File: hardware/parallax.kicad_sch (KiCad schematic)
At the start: 18 parts, among them U1 4052, U2 MCP6002-xMC

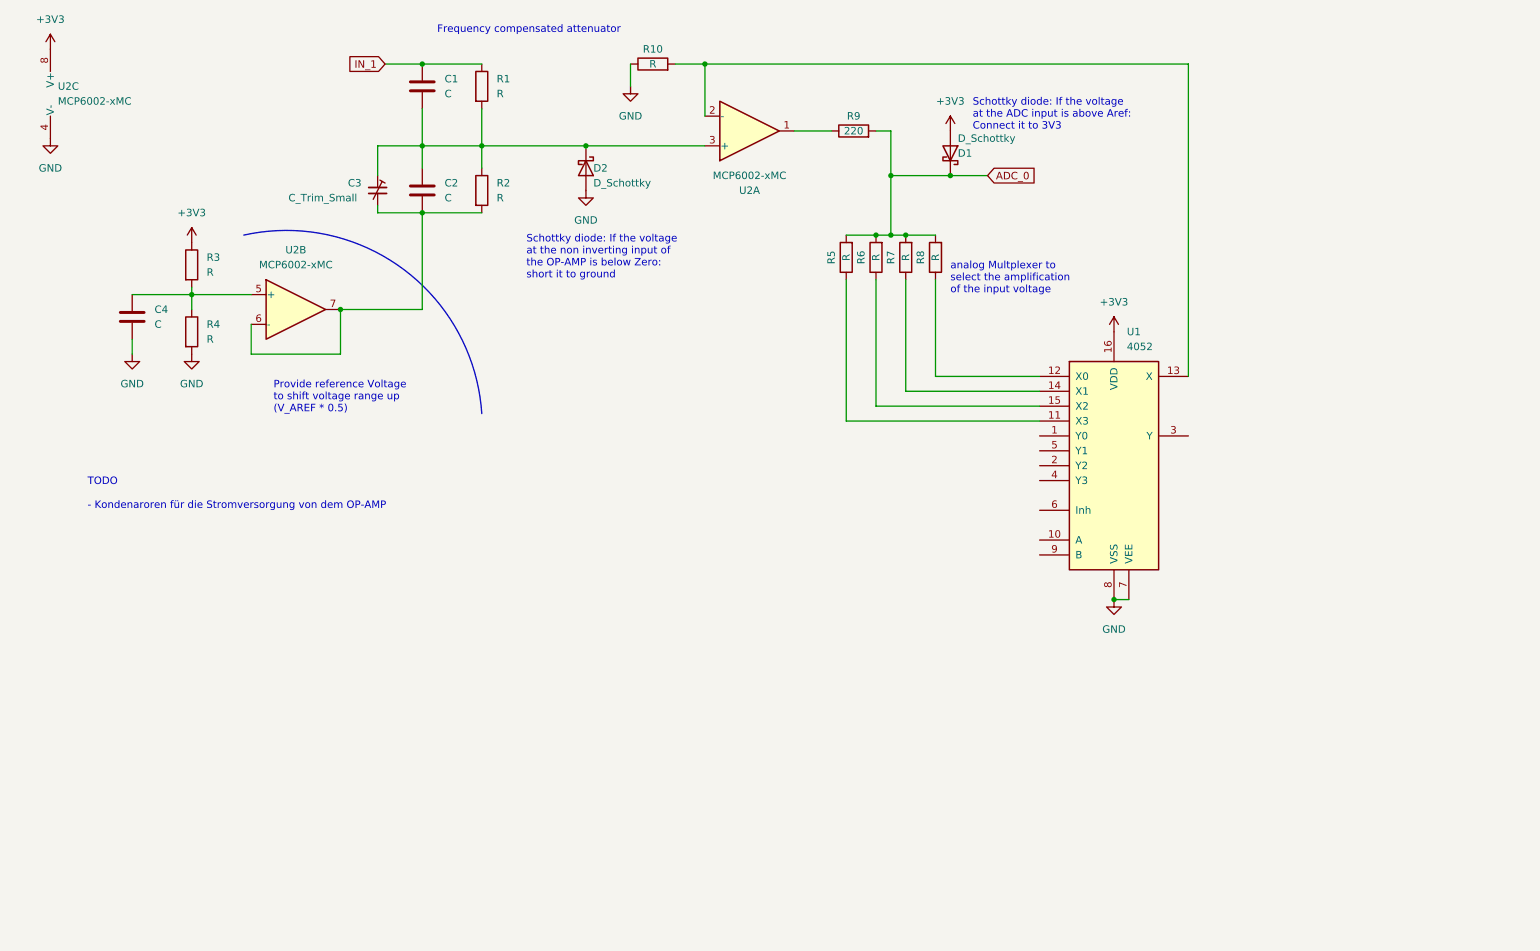
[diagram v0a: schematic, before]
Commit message: better structure of schematics
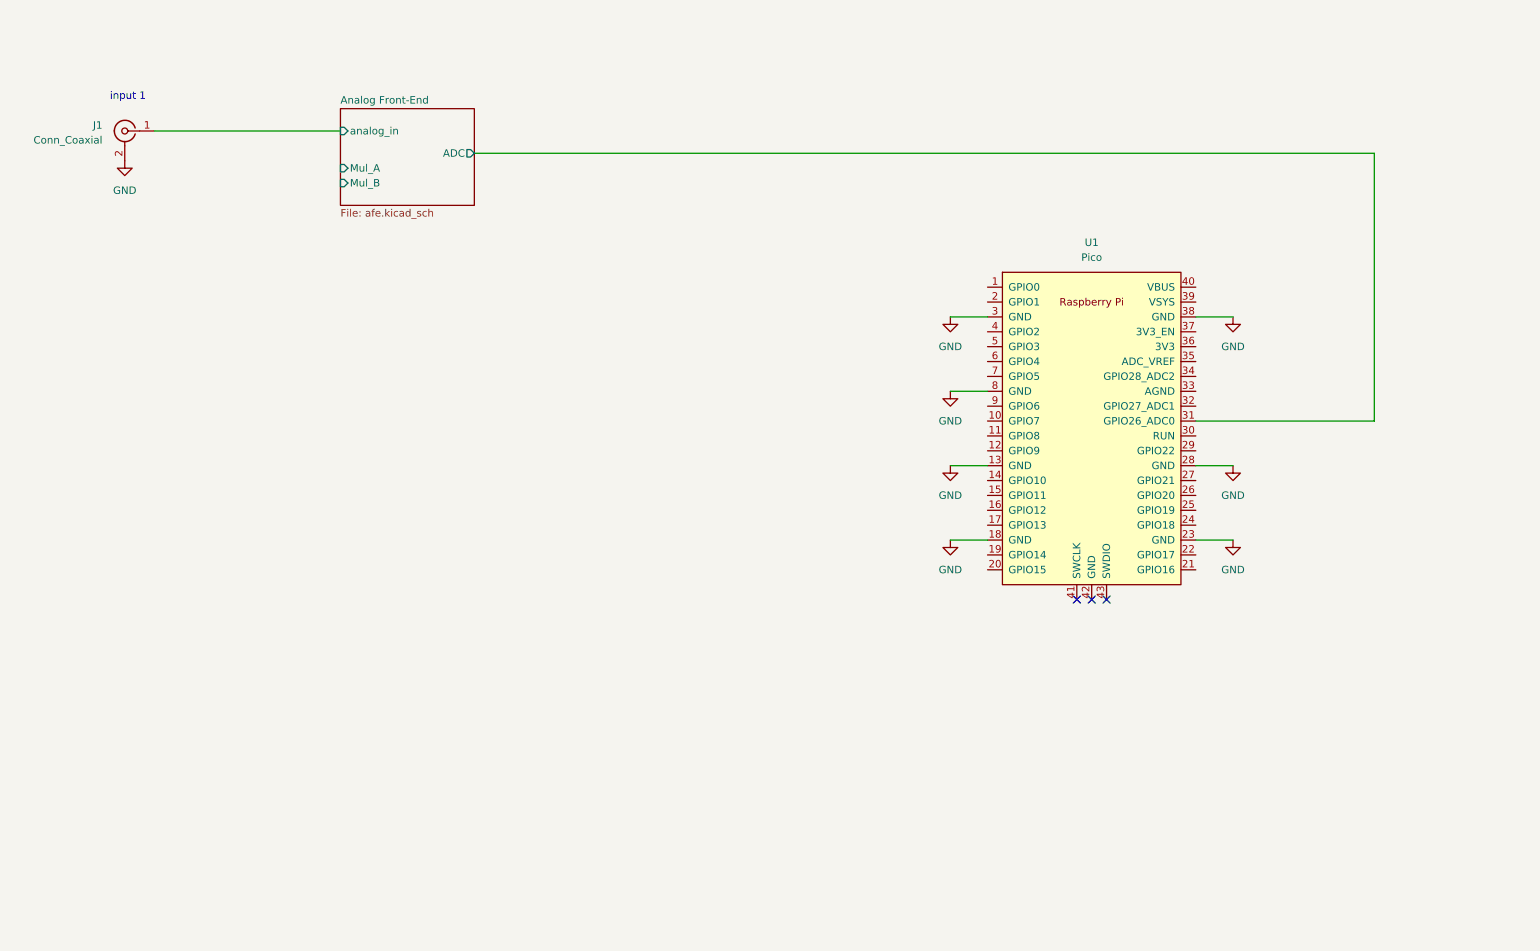
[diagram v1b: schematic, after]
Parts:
- removed C1, C2, C4: C, symbol Device:C
- removed C3: C_Trim_Small, symbol Device:C_Trim_Small
- removed D1, D2: D_Schottky, symbol Device:D_Schottky
- removed R1, R10, R2, R3, R4, R5, R6, R7, R8: R, symbol Device:R
- removed R9: 220, symbol Device:R
- removed U1: 4052, Package_SO:SSOP-16_5.3x6.2mm_P0.65mm, symbol 4xxx:4052
- removed U2: MCP6002-xMC, Package_DFN_QFN:DFN-8-1EP_3x2mm_P0.5mm_EP1.75x1.45mm, symbol Amplifier_Operational:MCP6002-xMC
- added J1: Conn_Coaxial, symbol Connector:Conn_Coaxial
- added U1: Pico, MCU_RaspberryPi_and_Boards:RPi_Pico_SMD_TH, symbol MCU_RaspberryPi_and_Boards:Pico
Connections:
- net GND: now also J1.2 (Ext), U1.13 (GND), U1.18 (GND), U1.23 (GND), U1.28 (GND), U1.3 (GND), U1.38 (GND), U1.8 (GND)
- new net Analog Front-End/ADC: U1.31 (GPIO26_ADC0)
- new net Analog Front-End/analog_in: J1.1 (In)
- no-connect marks 0 -> 3
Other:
- added sheet Analog Front-End (afe.kicad_sch)
- note added: "input 1"
- note removed: "Frequency compensated attenuator"
- note removed: "Provide reference Voltage to shift voltage range up (V_AREF * 0.5)"
- note removed: "Schottky diode: If the voltage at the ADC input is above Aref: Connect it to 3V3"
- note removed: "Schottky diode: If the voltage at the non inverting input of the OP-AMP is below Zero: short it to ground"
- note removed: "TODO - Kondenaroren für die Stromversorgung von dem OP-AMP"
- note removed: "analog Multplexer to select the amplification of the input voltage"

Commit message: started adding some footprints
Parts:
- J1: footprint (none) -> Connector_Coaxial:BNC_Amphenol_B6252HB-NPP3G-50_Horizontal
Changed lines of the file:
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@@
       (effects (font (size 1.27 1.27)) (justify left))
     )
-    (property "Footprint" "" (at 39.37 40.64 0)
+    (property "Footprint" "Connector_Coaxial:BNC_Amphenol_B6252HB-NPP3G-50_Horizontal" (at 39.37 40.64 0)
       (effects (font (size 1.27 1.27)) hide)
     )

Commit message: [hard] footprint assignment and some Part Ordering numbers
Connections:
- net +3V3: now reaches U1.36 (3V3)
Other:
- note added: "todo: add some status LEDs?"
- note added: "todo: maybe add a signal genertor? (R2R Ladder DAC 12 Bit?)"
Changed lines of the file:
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@@
+    (stroke (width 0) (type default))
+  )
+  (wire (pts (xy 222.25 77.47) (xy 232.41 77.47))
     (stroke (width 0) (type default))
   )
@@
   )
   (text "input 1" (at 36.83 35.56 0)
+    (effects (font (size 1.27 1.27)) (justify left bottom))
+  )
+  (text "todo: add some status LEDs?" (at 102.87 128.27 0)
+    (effects (font (size 1.27 1.27)) (justify left bottom))
+  )
+  (text "todo: maybe add a signal genertor?\n(R2R Ladder DAC 12 Bit?)"
+    (at 100.33 139.7 0)
     (effects (font (size 1.27 1.27)) (justify left bottom))
   )
@@
         )
       )
+    )
+  )
+  (symbol (lib_id "power:+3V3") (at 232.41 77.47 0) (unit 1)
+    (in_bom yes) (on_board yes) (dnp no) (fields_autoplaced)
+    (property "Reference" "#PWR025" (at 232.41 81.28 0)
+      (effects (font (size 1.27 1.27)) hide)
+    )
+    (property "Value" "+3V3" (at 232.41 72.39 0)
+      (effects (font (size 1.27 1.27)))
+    )
+    (property "Footprint" "" (at 232.41 77.47 0)
+      (effects (font (size 1.27 1.27)) hide)
+    )
+    (property "Datasheet" "" (at 232.41 77.47 0)
+      (effects (font (size 1.27 1.27)) hide)
+    )
+    (pin "1")
+    (instances
+      (project "parallax"
+        (path "/9be75e04-ffa7-400b-a6f6-98cbc4c2c88c"
+          (reference "#PWR025") (unit 1)
+        )
+      )

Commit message: restructured schematics, added more symbols and also some ordering part numbers
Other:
- note added: "TODO: - Status LEDs - Signal Generator? - Logic Analyser - Make all unused Pins available - Synchronize multiple oscilloscopes?"
- note removed: "todo: add some status LEDs?"
- note removed: "todo: maybe add a signal genertor? (R2R Ladder DAC 12 Bit?)"
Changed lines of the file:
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@@
+    (stroke (width 0) (type default))
+  )
+  (wire (pts (xy 222.25 77.47) (xy 242.57 77.47))
     (stroke (width 0) (type default))
   )
@@
     (stroke (width 0) (type default))
   )
-  (wire (pts (xy 222.25 77.47) (xy 232.41 77.47))
-    (stroke (width 0) (type default))
-  )
   (wire (pts (xy 222.25 97.79) (xy 228.6 97.79))
     (stroke (width 0) (type default))
@@
     (effects (font (size 1.27 1.27)) (justify left bottom))
   )
-  (text "todo: add some status LEDs?" (at 102.87 128.27 0)
-    (effects (font (size 1.27 1.27)) (justify left bottom))
-  )
-  (text "todo: maybe add a signal genertor?\n(R2R Ladder DAC 12 Bit?)"
-    (at 100.33 139.7 0)
-    (effects (font (size 1.27 1.27)) (justify left bottom))
+  (text "TODO:\n\n- Status LEDs\n- Signal Generator?\n- Logic Analyser\n- Make all unused Pins available\n	- Synchronize multiple oscilloscopes?"
+    (at 109.22 148.59 0)
+    (effects (font (size 1.27 1.27)) (justify left bottom))
+  )
+  (netclass_flag "" (length 2.54) (shape round) (at 226.06 72.39 0) (fields_autoplaced)
+    (effects (font (size 1.27 1.27)) (justify left bottom))
+    (property "Netclass" "Gnd" (at 226.7585 69.85 0)
+      (effects (font (size 1.27 1.27) italic) (justify left))
+    )
+  )
+  (netclass_flag "" (length 2.54) (shape round) (at 236.22 77.47 0) (fields_autoplaced)
+    (effects (font (size 1.27 1.27)) (justify left bottom))
+    (property "Netclass" "3V3" (at 236.9185 74.93 0)
+      (effects (font (size 1.27 1.27) italic) (justify left))
+    )
   )
   (symbol (lib_id "power:GND") (at 228.6 72.39 0) (unit 1)
@@
     )
   )
-  (symbol (lib_id "power:+3V3") (at 232.41 77.47 0) (unit 1)
-    (in_bom yes) (on_board yes) (dnp no) (fields_autoplaced)
-    (property "Reference" "#PWR025" (at 232.41 81.28 0)
-      (effects (font (size 1.27 1.27)) hide)
-    )
-    (property "Value" "+3V3" (at 232.41 72.39 0)
-      (effects (font (size 1.27 1.27)))
-    )
-    (property "Footprint" "" (at 232.41 77.47 0)
-      (effects (font (size 1.27 1.27)) hide)
-    )
-    (property "Datasheet" "" (at 232.41 77.47 0)
-      (effects (font (size 1.27 1.27)) hide)
-    )
+  (symbol (lib_id "power:+3V3") (at 242.57 77.47 0) (unit 1)
+    (in_bom yes) (on_board yes) (dnp no) (fields_autoplaced)
+    (property "Reference" "#PWR025" (at 242.57 81.28 0)
+      (effects (font (size 1.27 1.27)) hide)
+    )
+    (property "Value" "+3V3" (at 242.57 72.39 0)
+      (effects (font (size 1.27 1.27)))
+    )
+    (property "Footprint" "" (at 242.57 77.47 0)
+      (effects (font (size 1.27 1.27)) hide)
+    )
+    (property "Datasheet" "" (at 242.57 77.47 0)
+      (effects (font (size 1.27 1.27)) hide)
+    )

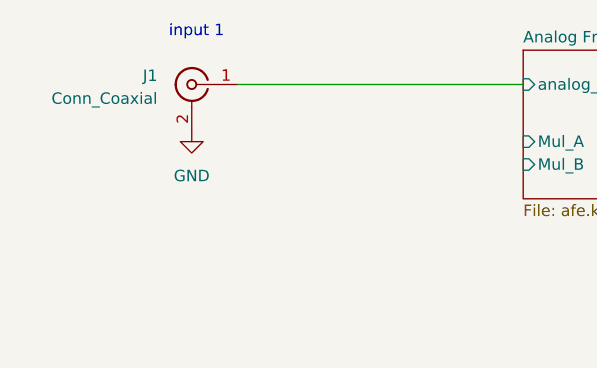
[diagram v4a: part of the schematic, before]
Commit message: update analog front-end and resistor calculator: Better documentation
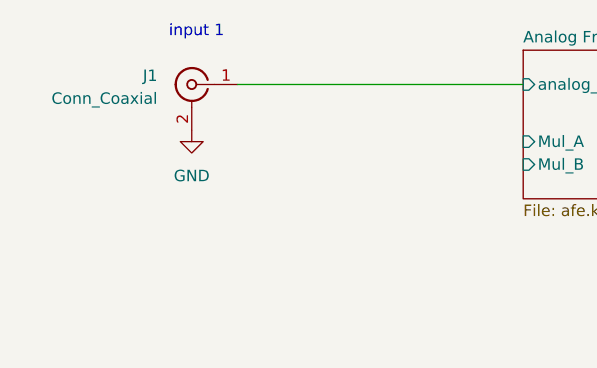
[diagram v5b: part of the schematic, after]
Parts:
- U1: footprint MCU_RaspberryPi_and_Boards:RPi_Pico_SMD_TH -> Module:RaspberryPi_Pico_Common_Unspecified

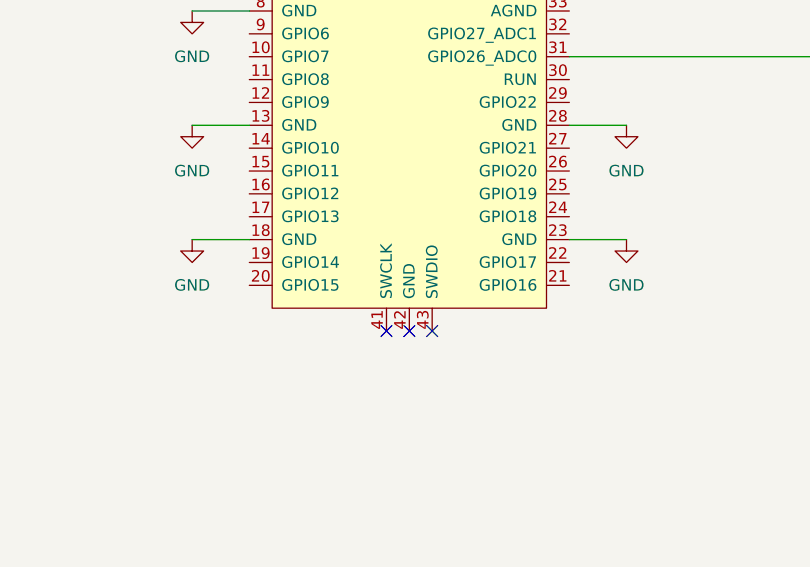
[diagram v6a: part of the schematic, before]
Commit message: afe and simulation ready
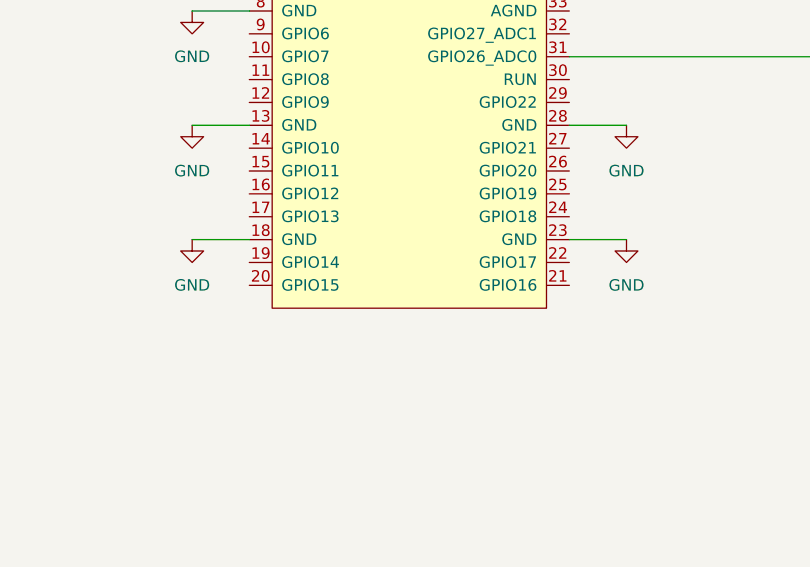
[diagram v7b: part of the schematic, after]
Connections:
- no-connect marks 3 -> 0
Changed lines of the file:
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@@
 		)
-	)
-	(no_connect
-		(at 207.01 120.65)
-	)
-	(no_connect
-		(at 201.93 120.65)
-	)
-	(no_connect
-		(at 204.47 120.65)
 	)
 	(wire
@@
 		(pin "36"
 		)
-		(pin "43"
-		)
 		(pin "40"
 		)
-		(pin "41"
-		)
 		(pin "39"
 		)
@@
 		(pin "29"
 		)
-		(pin "42"
-		)
 		(pin "8"

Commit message: started PCB routing, AFE ready, rest still in Progress
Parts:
- added C1: 100nF, Capacitor_SMD:C_0603_1608Metric, symbol Device:C
- added D1, D2: LED, LED_SMD:LED_0603_1608Metric_Pad1.05x0.95mm_HandSolder, symbol Device:LED
- added J2, J3: Conn_Coaxial, Connector_Coaxial:BNC_Amphenol_B6252HB-NPP3G-50_Horizontal, symbol Connector:Conn_Coaxial
- added J4: Conn_01x10_Pin, Connector_PinHeader_2.54mm:PinHeader_1x10_P2.54mm_Vertical, symbol Connector:Conn_01x10_Pin
- added J5: Conn_01x02_Pin, Connector_PinHeader_2.54mm:PinHeader_1x02_P2.54mm_Vertical, symbol Connector:Conn_01x02_Pin
- added R1, R2: 4K7, Resistor_SMD:R_0603_1608Metric, symbol Device:R
- added R3: 10K, Resistor_SMD:R_0603_1608Metric, symbol Device:R
- added R4: 1K, Resistor_SMD:R_0603_1608Metric, symbol Device:R
- added SW1: SW_Push_Dual, work:SW_PUSH-12mm, symbol Switch:SW_Push_Dual
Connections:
- net +3V3: now also R3.1
- net GND: now also U1.33 (AGND), C1.2, J2.2 (Ext), J3.2 (Ext), J4.1 (Pin_1), J4.10 (Pin_10), J5.1 (Pin_1), R1.1, R2.1, R4.2
- net R2R-DAC/B7: now reaches U1.1 (GPIO0)
- net R2R-DAC/B0: now reaches U1.10 (GPIO7)
- net at U1.11 (GPIO8): now also J4.2 (Pin_2)
- net at U1.12 (GPIO9): now also J4.3 (Pin_3)
- net at U1.14 (GPIO10): now also J4.4 (Pin_4)
- net at U1.15 (GPIO11): now also J4.5 (Pin_5)
- net at U1.16 (GPIO12): now also J4.6 (Pin_6)
- net at U1.17 (GPIO13): now also J4.7 (Pin_7)
- net at U1.19 (GPIO14): now also J4.8 (Pin_8)
- net R2R-DAC/B6: now reaches U1.2 (GPIO1)
- net at U1.20 (GPIO15): now also J4.9 (Pin_9)
- net at U1.21 (GPIO16): now also J5.2 (Pin_2)
- net LED_2: now reaches U1.22 (GPIO17)
- net LED_2: now also D2.2 (A)
- net MUL_2B: now reaches U1.24 (GPIO18)
- net MUL_2A: now reaches U1.25 (GPIO19)
- net MUL_1A: now reaches U1.26 (GPIO20)
- net MUL_1B: now reaches U1.27 (GPIO21)
- net LED_1: now reaches U1.29 (GPIO22)
- net LED_1: now also D1.2 (A)
- net Reset: now reaches U1.30 (RUN)
- net Reset: now also C1.1, R3.2, SW1.1, SW1.3
- net Analog Front-End1/ADC: now reaches U1.34 (GPIO28_ADC2)
- net R2R-DAC/B5: now reaches U1.4 (GPIO2)
- net R2R-DAC/B4: now reaches U1.5 (GPIO3)
- net R2R-DAC/B3: now reaches U1.6 (GPIO4)
- net R2R-DAC/B2: now reaches U1.7 (GPIO5)
- net R2R-DAC/B1: now reaches U1.9 (GPIO6)
- new net: R4.1, SW1.2, SW1.4
- new net: D2.1 (K), R2.2
- new net: D1.1 (K), R1.2
- new net Analog Front-End1/analog_in: J2.1 (In)
- new net R2R-DAC/AWG_OUT: J3.1 (In)
- no-connect marks 0 -> 5
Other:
- added sheet Analog Front-End1 (afe.kicad_sch)
- added sheet R2R-DAC (awg.kicad_sch)
- note added: "3V3_EN: low-active disable for onboard 3V3 regulator"
- note added: "Maybe this can be used for another purpose"
- note added: "PIO configured as square signal generator"
- note added: "TODO: - Square Signal Generator for calibration purposes - Logic Analyser - Synchronise Clocks"
- note added: "Unused IO Pins Maybe use as logic analyser"
- note added: "input 2"
- note removed: "TODO: - Status LEDs - Signal Generator? - Logic Analyser - Make all unused Pins available - Synchronize multiple oscilloscopes?"
- moved on the sheet: U1
